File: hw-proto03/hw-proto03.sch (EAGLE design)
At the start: 34 parts, among them IC2 IR4427S, IC3 MCP2562T, IC5 IR4427S, J1 J15MM, J2 J5MM, J3 J12MM, J4 J5MM, Q1 SQJ147ELP-T1_GE3, Q2 SQJ147ELP-T1_GE3, Q3 VN5E160MSTR-E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

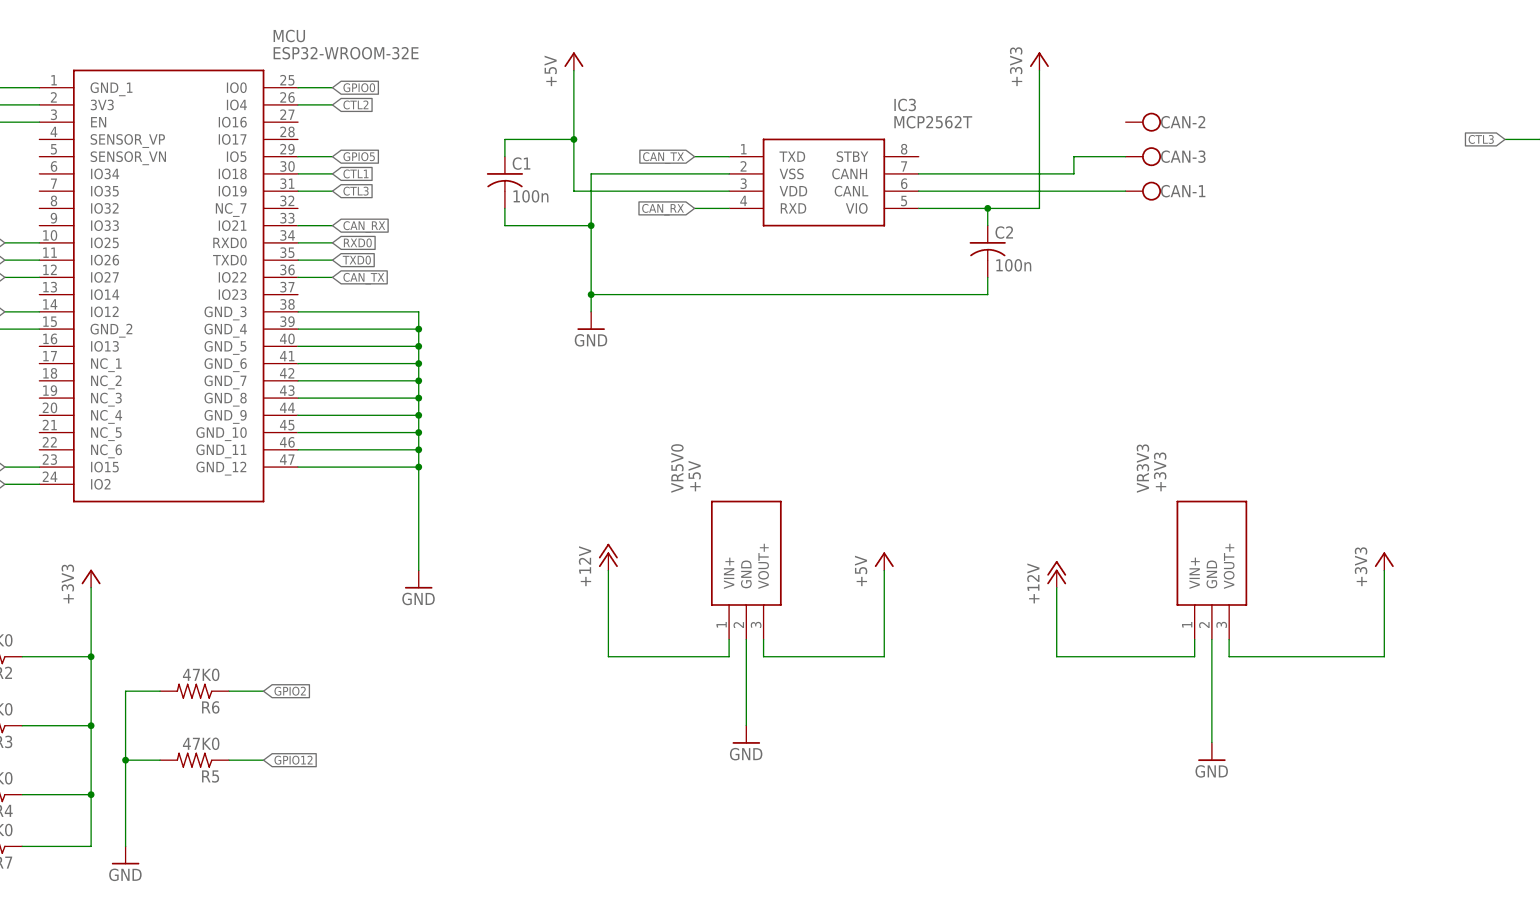
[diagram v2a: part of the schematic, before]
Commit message: 2nd pass layout and routing complete, needs optimizing
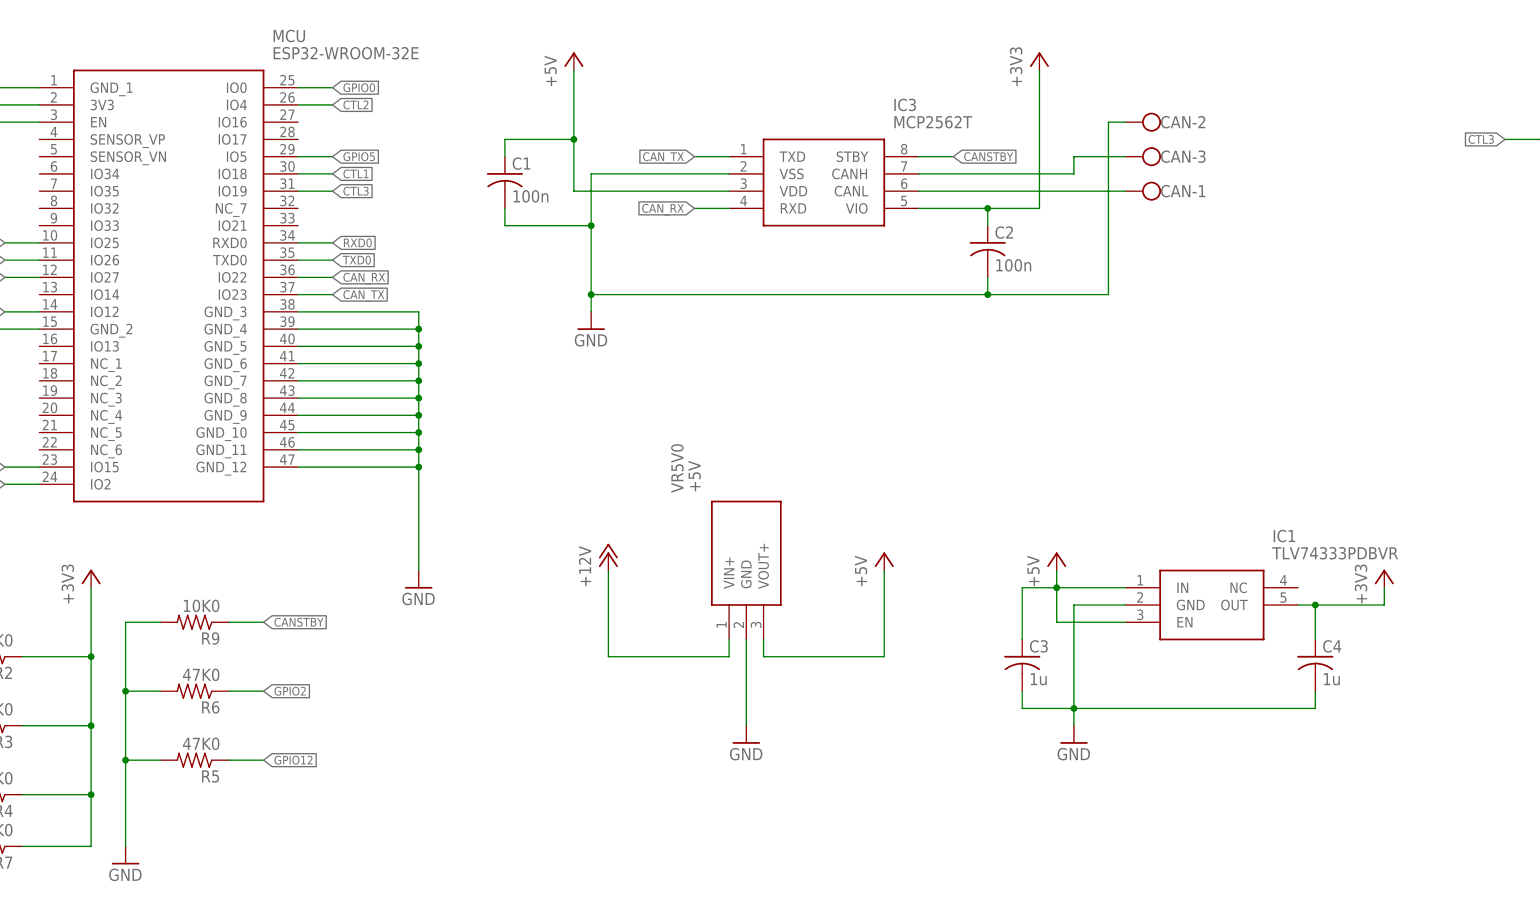
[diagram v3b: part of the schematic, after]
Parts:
- removed VR3V3: +3V3, TSR_1-2433E:TSR_1-2433E
- added C3, C4: 1u, rcl:C-USC0603K
- added IC1: TLV74333PDBVR, TLV74333PDBVR:TLV74333PDBVR
- added R9: 10K0, rcl:R-US_R0603
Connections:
- new net CANSTBY: IC3.STBY, R9.1
- net +12V: no longer VR3V3.VIN+
- net +3V3: now also C4.1, IC1.OUT; no longer VR3V3.VOUT+
- net +5V: now also C3.1, IC1.EN, IC1.IN
- net CAN_RX: now also MCU.IO22; no longer MCU.IO21
- net CAN_TX: now also MCU.IO23; no longer MCU.IO22
- net GND: now also C3.2, C4.2, CAN-2.KL, IC1.GND, R9.2; no longer VR3V3.GND
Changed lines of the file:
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@@
 <part name="GND4" library="supply1" deviceset="GND" device=""/>
 <part name="GND6" library="supply1" deviceset="GND" device=""/>
-<part name="VR3V3" library="TSR_1-2433E" deviceset="TSR_1-2433E" device="" value="+3V3"/>
 <part name="GND7" library="supply1" deviceset="GND" device=""/>
 <part name="+3V1" library="supply1" deviceset="+3V3" device=""/>
@@
 <part name="P+1" library="supply1" deviceset="+12V" device=""/>
 <part name="P+2" library="supply1" deviceset="+12V" device=""/>
-<part name="P+3" library="supply1" deviceset="+12V" device=""/>
 <part name="P+4" library="supply1" deviceset="+12V" device=""/>
 <part name="VR5V0" library="TSR_1-2433E" deviceset="TSR_1-2433E" device="" value="+5V"/>
@@
 <part name="J3" library="jumper" deviceset="J" device="12MM" value="J12MM"/>
 <part name="J4" library="jumper" deviceset="J" device="5MM"/>
+<part name="P+3" library="supply1" deviceset="+5V" device=""/>
+<part name="IC1" library="TLV74333PDBVR" deviceset="TLV74333PDBVR" device=""/>
+<part name="C3" library="rcl" deviceset="C-US" device="C0603K" value="1u"/>
+<part name="C4" library="rcl" deviceset="C-US" device="C0603K" value="1u"/>
+<part name="R9" library="rcl" deviceset="R-US_" device="R0603" value="10K0"/>
 </parts>
 <sheets>
@@
 <instance part="GND4" gate="1" x="238.76" y="106.68"/>
 <instance part="GND6" gate="1" x="76.2" y="190.5"/>
-<instance part="VR3V3" gate="G$1" x="165.1" y="144.78" rot="R90"/>
-<instance part="GND7" gate="1" x="167.64" y="127"/>
-<instance part="+3V1" gate="G$1" x="193.04" y="157.48"/>
+<instance part="GND7" gate="1" x="147.32" y="129.54"/>
+<instance part="+3V1" gate="G$1" x="193.04" y="154.94"/>
 <instance part="+3V2" gate="G$1" x="-50.8" y="256.54"/>
 <instance part="P+1" gate="1" x="-10.16" y="93.98"/>
 <instance part="P+2" gate="1" x="238.76" y="137.16"/>
-<instance part="P+3" gate="1" x="144.78" y="154.94"/>
 <instance part="P+4" gate="1" x="78.74" y="157.48"/>
 <instance part="VR5V0" gate="G$1" x="96.52" y="144.78" rot="R90"/>
@@
 <instance part="J3" gate="1" x="132.08" y="58.42" rot="R90"/>
 <instance part="J4" gate="1" x="170.18" y="55.88" rot="R90"/>
+<instance part="P+3" gate="1" x="144.78" y="157.48"/>
+<instance part="IC1" gate="G$1" x="154.94" y="152.4"/>
+<instance part="C3" gate="G$1" x="139.7" y="142.24"/>
+<instance part="C4" gate="G$1" x="182.88" y="142.24"/>
+<instance part="R9" gate="G$1" x="17.78" y="147.32" rot="R180"/>
 </instances>
 <busses>
@@
 <wire x1="134.62" y1="195.58" x2="76.2" y2="195.58" width="0.1524" layer="91"/>
 <junction x="76.2" y="195.58"/>
-</segment>
-<segment>
-<pinref part="VR3V3" gate="G$1" pin="GND"/>
+<pinref part="CAN" gate="-2" pin="KL"/>
+<wire x1="154.94" y1="220.98" x2="152.4" y2="220.98" width="0.1524" layer="91"/>
+<wire x1="152.4" y1="220.98" x2="152.4" y2="195.58" width="0.1524" layer="91"/>
+<wire x1="152.4" y1="195.58" x2="134.62" y2="195.58" width="0.1524" layer="91"/>
+<junction x="134.62" y="195.58"/>
+</segment>
+<segment>
 <pinref part="GND7" gate="1" pin="GND"/>
-<wire x1="167.64" y1="144.78" x2="167.64" y2="129.54" width="0.1524" layer="91"/>
+<wire x1="147.32" y1="149.86" x2="147.32" y2="134.62" width="0.1524" layer="91"/>
+<pinref part="IC1" gate="G$1" pin="GND"/>
+<wire x1="147.32" y1="134.62" x2="147.32" y2="132.08" width="0.1524" layer="91"/>
+<wire x1="154.94" y1="149.86" x2="147.32" y2="149.86" width="0.1524" layer="91"/>
+<pinref part="C3" gate="G$1" pin="2"/>
+<wire x1="147.32" y1="134.62" x2="139.7" y2="134.62" width="0.1524" layer="91"/>
+<wire x1="139.7" y1="134.62" x2="139.7" y2="137.16" width="0.1524" layer="91"/>
+<junction x="147.32" y="134.62"/>
+<pinref part="C4" gate="G$1" pin="2"/>
+<wire x1="147.32" y1="134.62" x2="182.88" y2="134.62" width="0.1524" layer="91"/>
+<wire x1="182.88" y1="134.62" x2="182.88" y2="137.16" width="0.1524" layer="91"/>
 </segment>
 <segment>
@@
 <wire x1="7.62" y1="137.16" x2="7.62" y2="127" width="0.1524" layer="91"/>
 <junction x="7.62" y="127"/>
+<pinref part="R9" gate="G$1" pin="2"/>
+<wire x1="12.7" y1="147.32" x2="7.62" y2="147.32" width="0.1524" layer="91"/>
+<wire x1="7.62" y1="147.32" x2="7.62" y2="137.16" width="0.1524" layer="91"/>
+<junction x="7.62" y="137.16"/>
 </segment>
 <segment>
@@
 <net name="+3V3" class="0">
 <segment>
-<pinref part="VR3V3" gate="G$1" pin="VOUT+"/>
-<wire x1="170.18" y1="144.78" x2="170.18" y2="142.24" width="0.1524" layer="91"/>
-<pinref part="+3V1" gate="G$1" pin="+3V3"/>
-<wire x1="170.18" y1="142.24" x2="193.04" y2="142.24" width="0.1524" layer="91"/>
-<wire x1="193.04" y1="142.24" x2="193.04" y2="154.94" width="0.1524" layer="91"/>
-</segment>
-<segment>
 <pinref part="MCU" gate="G$1" pin="3V3"/>
 <pinref part="+3V2" gate="G$1" pin="+3V3"/>
@@
 <wire x1="-7.62" y1="142.24" x2="2.54" y2="142.24" width="0.1524" layer="91"/>
 <junction x="2.54" y="142.24"/>
+</segment>
+<segment>
+<pinref part="IC1" gate="G$1" pin="OUT"/>
+<pinref part="+3V1" gate="G$1" pin="+3V3"/>
+<wire x1="180.34" y1="149.86" x2="182.88" y2="149.86" width="0.1524" layer="91"/>
+<wire x1="182.88" y1="149.86" x2="193.04" y2="149.86" width="0.1524" layer="91"/>
+<wire x1="193.04" y1="149.86" x2="193.04" y2="152.4" width="0.1524" layer="91"/>
+<pinref part="C4" gate="G$1" pin="1"/>
+<wire x1="182.88" y1="144.78" x2="182.88" y2="149.86" width="0.1524" layer="91"/>
+<junction x="182.88" y="149.86"/>
 </segment>
 </net>
@@
 </segment>
 <segment>
-<wire x1="144.78" y1="152.4" x2="144.78" y2="142.24" width="0.1524" layer="91"/>
-<pinref part="VR3V3" gate="G$1" pin="VIN+"/>
-<wire x1="144.78" y1="142.24" x2="165.1" y2="142.24" width="0.1524" layer="91"/>
-<wire x1="165.1" y1="142.24" x2="165.1" y2="144.78" width="0.1524" layer="91"/>
-<pinref part="P+3" gate="1" pin="+12V"/>
-</segment>
-<segment>
 <pinref part="VR5V0" gate="G$1" pin="VIN+"/>
 <wire x1="96.52" y1="144.78" x2="96.52" y2="142.24" width="0.1524" layer="91"/>
@@
 <junction x="73.66" y="218.44"/>
 </segment>
+<segment>
+<pinref part="IC1" gate="G$1" pin="IN"/>
+<pinref part="P+3" gate="1" pin="+5V"/>
+<wire x1="154.94" y1="152.4" x2="144.78" y2="152.4" width="0.1524" layer="91"/>
+<wire x1="144.78" y1="152.4" x2="144.78" y2="154.94" width="0.1524" layer="91"/>
+<pinref part="IC1" gate="G$1" pin="EN"/>
+<wire x1="154.94" y1="147.32" x2="144.78" y2="147.32" width="0.1524" layer="91"/>
+<wire x1="144.78" y1="147.32" x2="144.78" y2="152.4" width="0.1524" layer="91"/>
+<junction x="144.78" y="152.4"/>
+<pinref part="C3" gate="G$1" pin="1"/>
+<wire x1="144.78" y1="152.4" x2="139.7" y2="152.4" width="0.1524" layer="91"/>
+<wire x1="139.7" y1="152.4" x2="139.7" y2="144.78" width="0.1524" layer="91"/>
+</segment>
 </net>
 <net name="CTL4" class="0">
@@
 </segment>
 <segment>
+<pinref part="MCU" gate="G$1" pin="IO23"/>
+<wire x1="38.1" y1="195.58" x2="33.02" y2="195.58" width="0.1524" layer="91"/>
+<label x="38.1" y="195.58" size="1.27" layer="95" xref="yes"/>
+</segment>
+</net>
+<net name="CAN_RX" class="0">
+<segment>
+<pinref part="IC3" gate="G$1" pin="RXD"/>
+<wire x1="91.44" y1="208.28" x2="96.52" y2="208.28" width="0.1524" layer="91"/>
+<label x="91.44" y="208.28" size="1.27" layer="95" rot="R180" xref="yes"/>
+</segment>
+<segment>
 <pinref part="MCU" gate="G$1" pin="IO22"/>
 <wire x1="38.1" y1="198.12" x2="33.02" y2="198.12" width="0.1524" layer="91"/>
 <label x="38.1" y="198.12" size="1.27" layer="95" xref="yes"/>
-</segment>
-</net>
-<net name="CAN_RX" class="0">
-<segment>
-<pinref part="IC3" gate="G$1" pin="RXD"/>
-<wire x1="91.44" y1="208.28" x2="96.52" y2="208.28" width="0.1524" layer="91"/>
-<label x="91.44" y="208.28" size="1.27" layer="95" rot="R180" xref="yes"/>
-</segment>
-<segment>
-<pinref part="MCU" gate="G$1" pin="IO21"/>
-<wire x1="38.1" y1="205.74" x2="33.02" y2="205.74" width="0.1524" layer="91"/>
-<label x="38.1" y="205.74" size="1.27" layer="95" xref="yes"/>
 </segment>
 </net>
@@
 </segment>
 </net>
+<net name="CANSTBY" class="0">
+<segment>
+<pinref part="IC3" gate="G$1" pin="STBY"/>
+<wire x1="129.54" y1="215.9" x2="124.46" y2="215.9" width="0.1524" layer="91"/>
+<label x="129.54" y="215.9" size="1.27" layer="95" xref="yes"/>
+</segment>
+<segment>
+<pinref part="R9" gate="G$1" pin="1"/>
+<wire x1="27.94" y1="147.32" x2="22.86" y2="147.32" width="0.1524" layer="91"/>
+<label x="27.94" y="147.32" size="1.27" layer="95" xref="yes"/>
+</segment>
+</net>
